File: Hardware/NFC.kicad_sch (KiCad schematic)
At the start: 7 parts, among them IC1 ST25DV04K-IER6S3

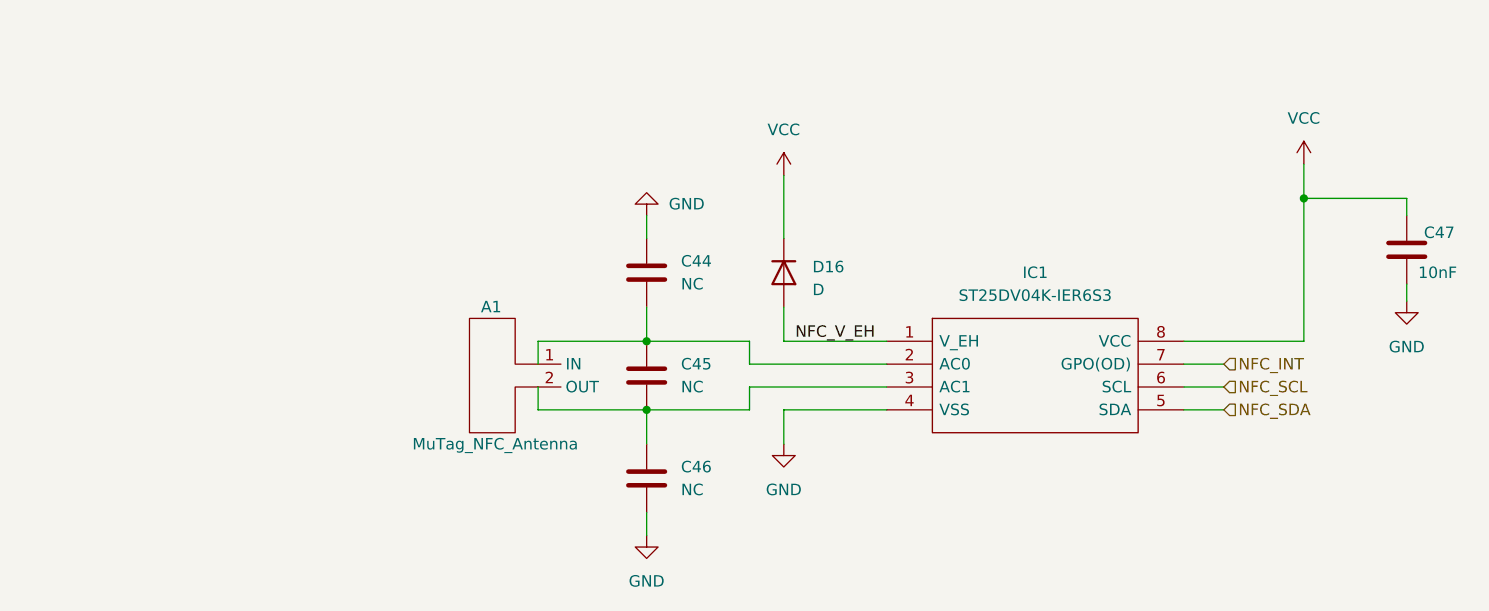
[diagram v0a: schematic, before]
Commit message: WIP - Added NFC Antenna and connected almost everythings else
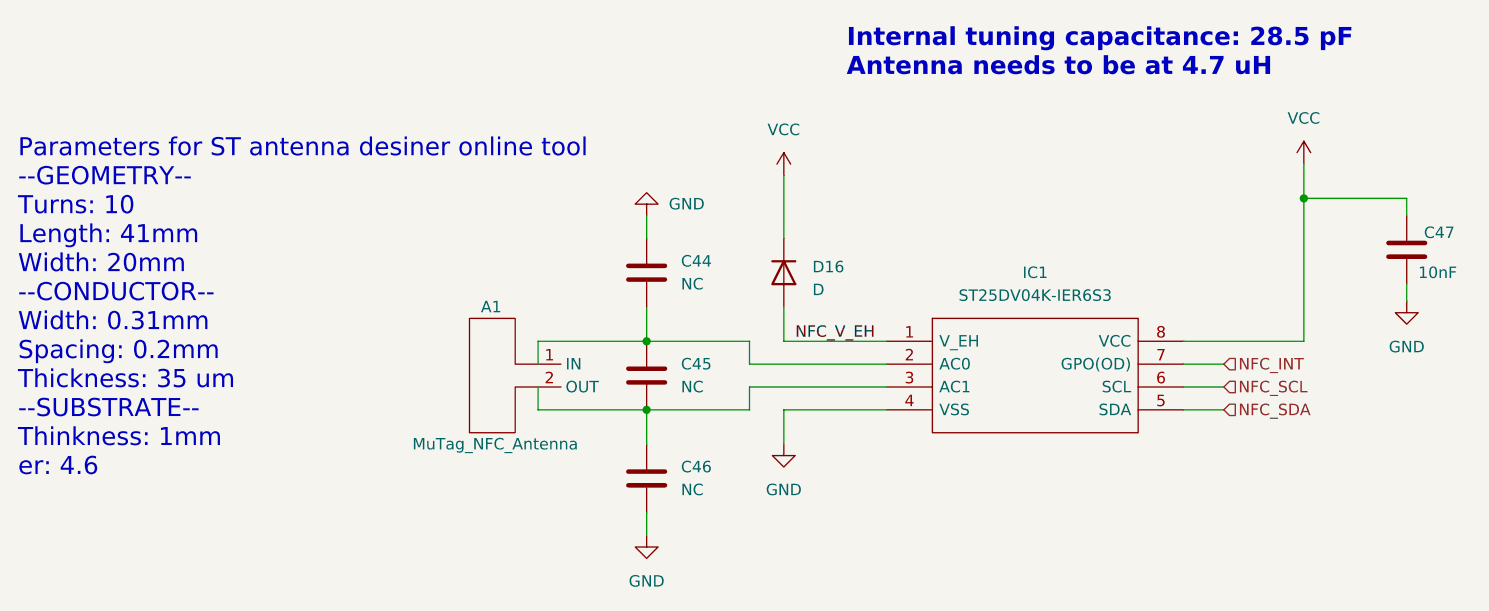
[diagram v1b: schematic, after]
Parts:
- A1: footprint (none) -> MuHack Badge NFC Antenna:muhack_badge_antenna
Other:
- note added: "Internal tuning capacitance: 28.5 pF Antenna needs to be at 4.7 uH"
- note added: "Parameters for ST antenna desiner online tool --GEOMETRY-- Turns: 10 Length: 41mm Width: 20mm --CONDUCTOR-- Width: 0.31mm Spacing: 0.2mm Thickness: 35 um --SUBSTRATE-- Thinkness: 1mm er: 4.6"
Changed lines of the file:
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@@
     (stroke (width 0) (type default))
+  )
+  (text "Internal tuning capacitance: 28.5 pF\nAntenna needs to be at 4.7 uH"
+    (at 113.03 46.355 0)
+    (effects (font (size 2 2) (thickness 0.4) bold) (justify left bottom))
+  )
+  (text "Parameters for ST antenna desiner online tool\n--GEOMETRY--\nTurns: 10\nLength: 41mm\nWidth: 20mm\n--CONDUCTOR--\nWidth: 0.31mm\nSpacing: 0.2mm\nThickness: 35 um\n--SUBSTRATE--\nThinkness: 1mm\ner: 4.6\n"
+    (at 20.955 90.805 0)
+    (effects (font (size 2 2)) (justify left bottom) (href "https://eds.st.com/antenna/#/"))
   )
   (label "NFC_V_EH" (at 107.315 75.565 0) (fields_autoplaced)
@@
       (effects (font (size 1.27 1.27)) (justify left))
     )
-    (property "Footprint" "" (at 80.01 78.105 0)
-      (effects (font (size 1.27 1.27)) hide)
-    )
+    (property "Footprint" "MuHack Badge NFC  Antenna:muhack_badge_antenna" (at 80.01 78.105 0)
+      (effects (font (size 1.27 1.27)) hide)
+    )

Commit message: TODO list completed - need to search for components
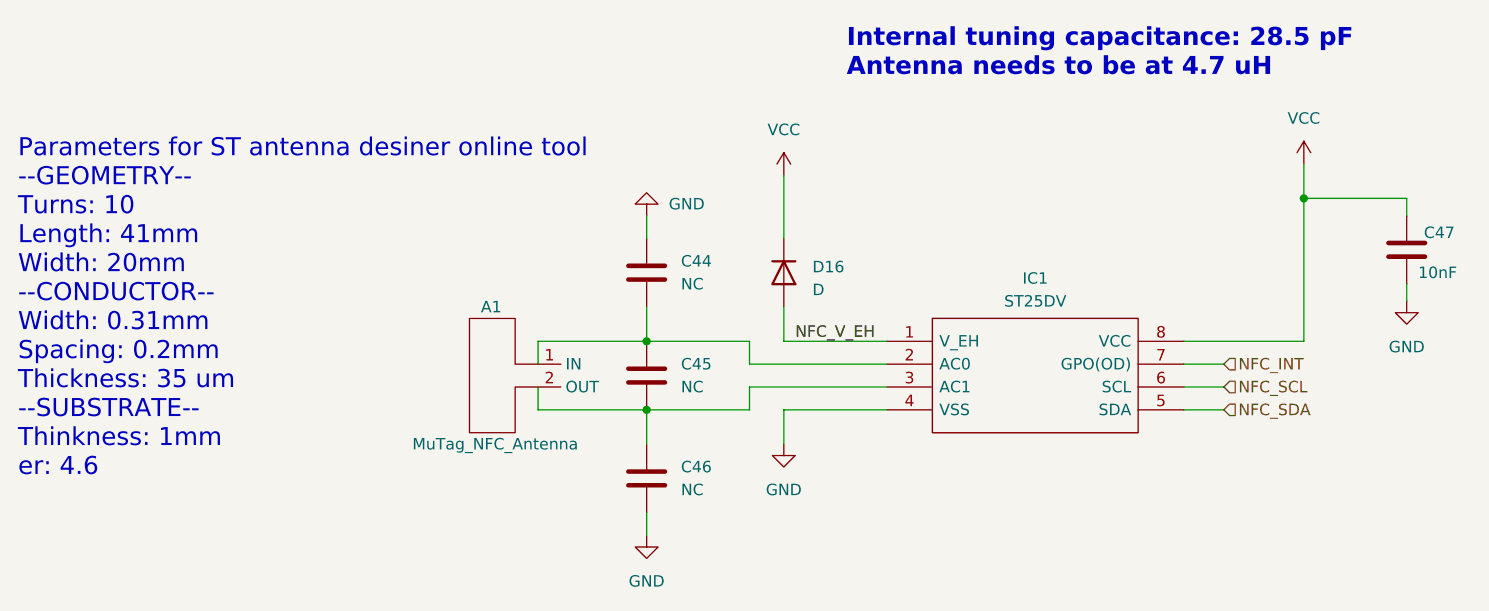
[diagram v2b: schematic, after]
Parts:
- IC1: value ST25DV04K-IER6S3 -> ST25DV
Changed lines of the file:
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@@
   (symbol (lib_id "ST25DV04K-IER6S3:ST25DV04K-IER6S3") (at 117.475 75.565 0) (unit 1)
     (in_bom yes) (on_board yes) (dnp no) (fields_autoplaced)
-    (property "Reference" "IC1" (at 133.985 67.945 0)
+    (property "Reference" "IC1" (at 133.985 68.58 0)
       (effects (font (size 1.27 1.27)))
     )
-    (property "Value" "ST25DV04K-IER6S3" (at 133.985 70.485 0)
+    (property "Value" "ST25DV" (at 133.985 71.12 0)
       (effects (font (size 1.27 1.27)))
     )

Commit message: Reworked the power system - ORDERED ON JLCPCB
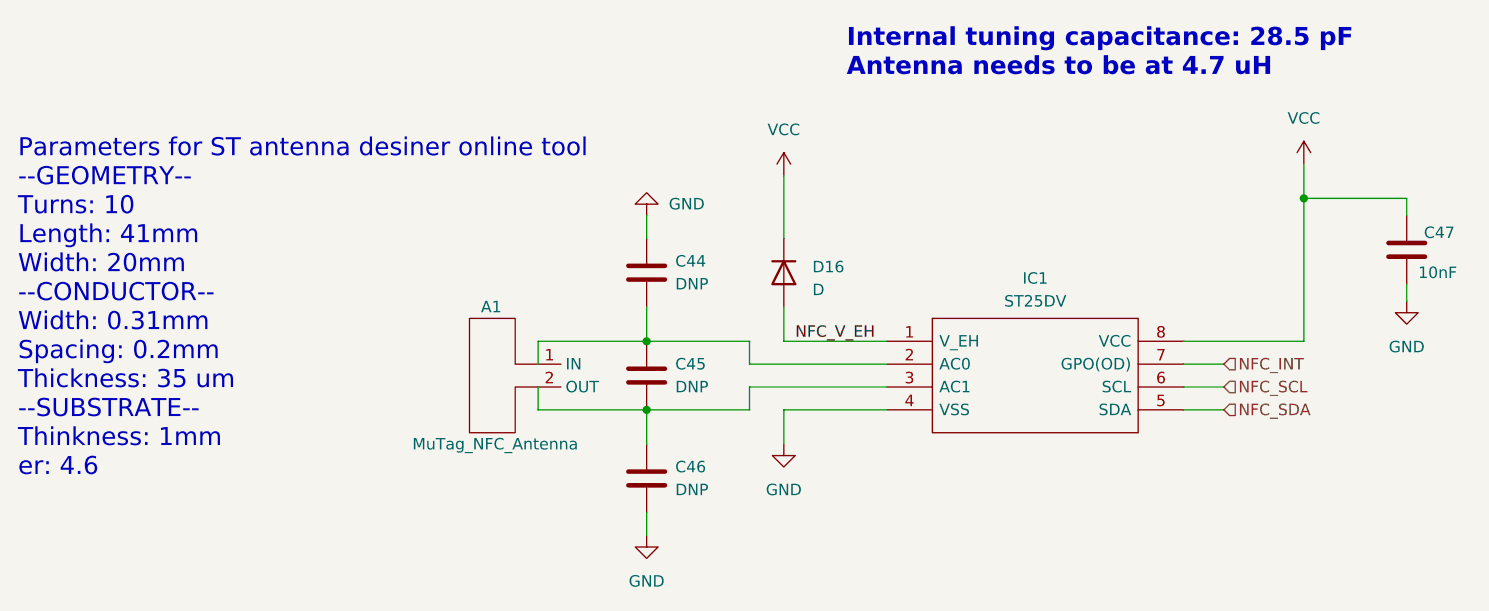
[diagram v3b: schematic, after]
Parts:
- C44, C45, C46: value NC -> DNP
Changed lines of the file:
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@@
   (symbol (lib_id "Device:C") (at 90.805 90.805 0) (unit 1)
     (in_bom yes) (on_board yes) (dnp no) (fields_autoplaced)
-    (property "Reference" "C46" (at 94.615 89.5349 0)
-      (effects (font (size 1.27 1.27)) (justify left))
-    )
-    (property "Value" "NC" (at 94.615 92.0749 0)
+    (property "Reference" "C46" (at 93.98 89.535 0)
+      (effects (font (size 1.27 1.27)) (justify left))
+    )
+    (property "Value" "DNP" (at 93.98 92.075 0)
       (effects (font (size 1.27 1.27)) (justify left))
     )
@@
   (symbol (lib_id "Device:C") (at 90.805 79.375 0) (unit 1)
     (in_bom yes) (on_board yes) (dnp no) (fields_autoplaced)
-    (property "Reference" "C45" (at 94.615 78.1049 0)
-      (effects (font (size 1.27 1.27)) (justify left))
-    )
-    (property "Value" "NC" (at 94.615 80.6449 0)
+    (property "Reference" "C45" (at 93.98 78.105 0)
+      (effects (font (size 1.27 1.27)) (justify left))
+    )
+    (property "Value" "DNP" (at 93.98 80.645 0)
       (effects (font (size 1.27 1.27)) (justify left))
     )
@@
   (symbol (lib_id "Device:C") (at 90.805 67.945 0) (unit 1)
     (in_bom yes) (on_board yes) (dnp no) (fields_autoplaced)
-    (property "Reference" "C44" (at 94.615 66.6749 0)
-      (effects (font (size 1.27 1.27)) (justify left))
-    )
-    (property "Value" "NC" (at 94.615 69.2149 0)
-      (effects (font (size 1.27 1.27)) (justify left))
-    )
+    (property "Reference" "C44" (at 93.98 66.675 0)
+      (effects (font (size 1.27 1.27)) (justify left))
+    )
+    (property "Value" "DNP" (at 93.98 69.215 0)
+      (effects (font (size 1.27 1.27)) (justify left))
+    )
